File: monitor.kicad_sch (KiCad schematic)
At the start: 0 parts

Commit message: monitor changes
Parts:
- added R5: R, symbol Device:R
- added SW2: SW_Wuerth_450301014042, Button_Switch_THT:SW_Slide-03_Wuerth-WS-SLTV_10x2.5x6.4_P2.54mm, symbol Switch:SW_Wuerth_450301014042
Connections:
- net M_VIN: now also R5.1
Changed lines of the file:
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@@
 	(wire
 		(pts
-			(xy 88.9 104.14) (xy 125.73 104.14)
-		)
-		(stroke
-			(width 0)
-			(type default)
-		)
-	)
-	(wire
-		(pts
-			(xy 125.73 104.14) (xy 125.73 69.85)
+			(xy 88.9 104.14) (xy 143.51 104.14)
+		)
+		(stroke
+			(width 0)
+			(type default)
+		)
+	)
+	(wire
+		(pts
+			(xy 143.51 104.14) (xy 143.51 69.85)
 		)
 		(stroke
@@
 	(hierarchical_label "M_A1V"
 		(shape output)
-		(at 107.95 69.85 90)
+		(at 125.73 69.85 90)
 		(effects
 			(font
@@
 	(hierarchical_label "M_A2V"
 		(shape input)
-		(at 125.73 69.85 90)
+		(at 143.51 69.85 90)
 		(effects
 			(font
@@
 		)
 	)
+	(symbol
+		(lib_id "Switch:SW_Wuerth_450301014042")
+		(at 109.22 81.28 0)
+		(unit 1)
+		(exclude_from_sim no)
+		(in_bom yes)
+		(on_board yes)
+		(dnp no)
+		(fields_autoplaced yes)
+		(property "Reference" "SW2"
+			(at 109.22 72.39 0)
+			(effects
+				(font
+					(size 1.27 1.27)
+				)
+			)
+		)
+		(property "Value" "SW_Wuerth_450301014042"
+			(at 109.22 74.93 0)
+			(effects
+				(font
+					(size 1.27 1.27)
+				)
+			)
+		)
+		(property "Footprint" "Button_Switch_THT:SW_Slide-03_Wuerth-WS-SLTV_10x2.5x6.4_P2.54mm"
+			(at 109.22 91.44 0)
+			(effects
+				(font
+					(size 1.27 1.27)
+				)
+				(hide yes)
+			)
+		)
+		(property "Datasheet" "https://www.we-online.com/components/products/datasheet/450301014042.pdf"
+			(at 109.22 88.9 0)
+			(effects
+				(font
+					(size 1.27 1.27)
+				)
+				(hide yes)
+			)
+		)
+		(property "Description" "Switch slide, single pole double throw"
+			(at 109.22 81.28 0)
+			(effects
+				(font
+					(size 1.27 1.27)
+				)
+				(hide yes)
+			)
+		)
+		(pin "1"
+		)
+		(pin "2"
+		)
+		(pin "3"
+		)
+		(instances
+			(project ""
+				(path "/bdc7face-9f7c-4701-80bb-4cc144448db1/10220f6e-30e0-4da2-bc7c-0672de199a7a"
+					(reference "SW2")
+					(unit 1)
+				)
+			)
+		)
+	)
+	(symbol
+		(lib_id "Device:R")
+		(at 92.71 81.28 90)
+		(unit 1)
+		(exclude_from_sim no)
+		(in_bom yes)
+		(on_board yes)
+		(dnp no)
+		(fields_autoplaced yes)
+		(property "Reference" "R5"
+			(at 92.71 74.93 90)
+			(effects
+				(font
+					(size 1.27 1.27)
+				)
+			)
+		)
+		(property "Value" "R"
+			(at 92.71 77.47 90)
+			(effects
+				(font
+					(size 1.27 1.27)
+				)
+			)
+		)
+		(property "Footprint" ""
+			(at 92.71 83.058 90)
+			(effects
+				(font
+					(size 1.27 1.27)
+				)
+				(hide yes)
+			)
+		)
+		(property "Datasheet" "~"
+			(at 92.71 81.28 0)
+			(effects
+				(font
+					(size 1.27 1.27)
+				)
+				(hide yes)
+			)
+		)
+		(property "Description" "Resistor"
+			(at 92.71 81.28 0)
+			(effects
+				(font
+					(size 1.27 1.27)
+				)
+				(hide yes)
+			)
+		)
+		(pin "2"
+		)
+		(pin "1"
+		)
+		(instances
+			(project ""
+				(path "/bdc7face-9f7c-4701-80bb-4cc144448db1/10220f6e-30e0-4da2-bc7c-0672de199a7a"
+					(reference "R5")
+					(unit 1)
+				)
+			)
+		)
+	)

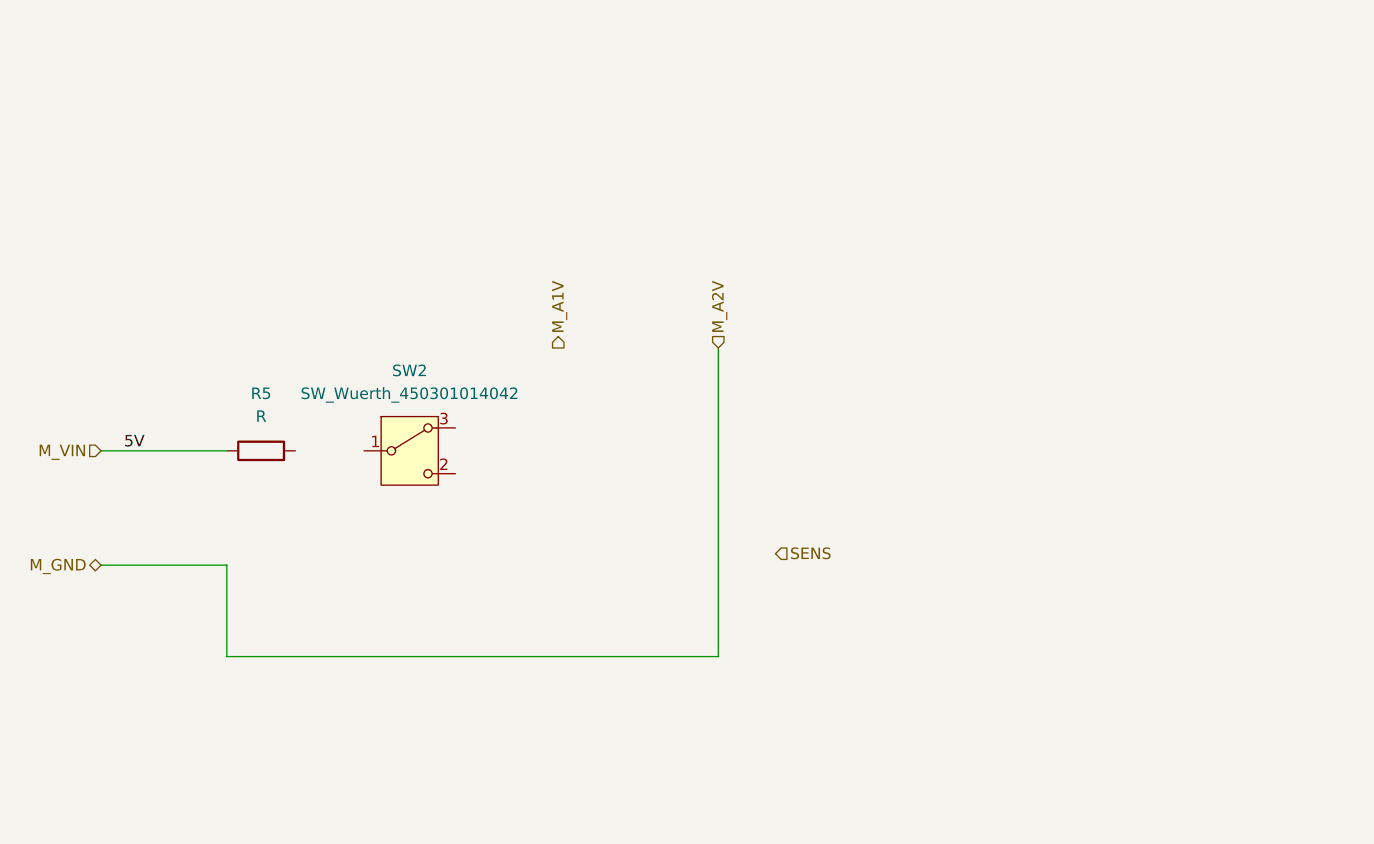
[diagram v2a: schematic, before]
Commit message: monitor internals: temporary solution
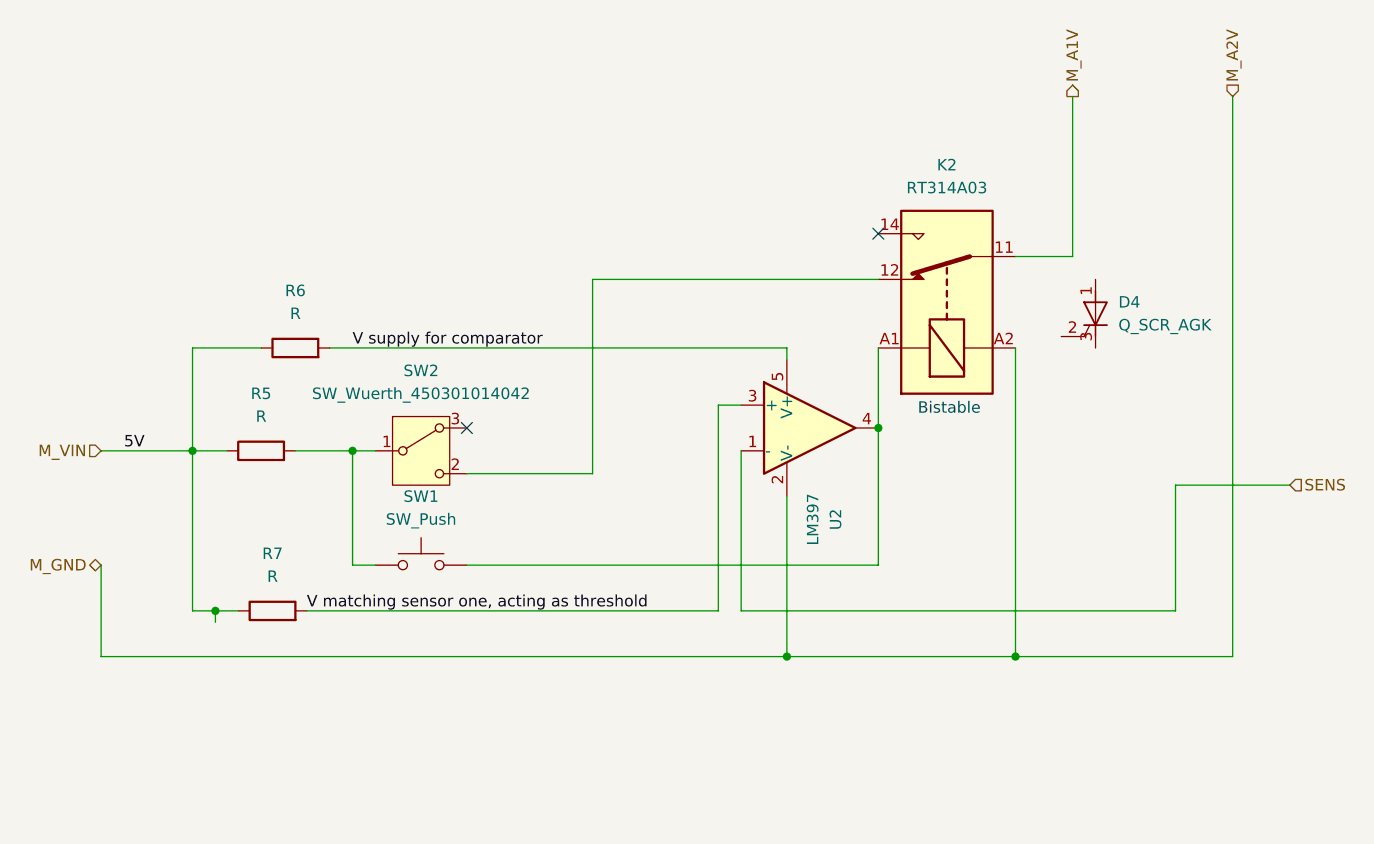
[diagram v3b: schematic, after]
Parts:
- added D4: Q_SCR_AGK, symbol Device:Q_SCR_AGK
- added K2: RT314A03, Relay_THT:Relay_SPDT_Schrack-RT1-16A-FormC_RM5mm, symbol Relay:RT314A05
- added R6, R7: R, symbol Device:R
- added SW1: SW_Push, symbol Switch:SW_Push
- added U2: LM397, Package_TO_SOT_SMD:SOT-23-5, symbol Comparator:LM397
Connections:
- net M_A1V: now also K2.11
- net M_A2V: now also K2.A2, U2.2 (V-)
- net M_VIN: now also R6.1, R7.1
- net SENS: now also U2.1 (-)
- net at SW2.1 (B): now also R5.2, SW1.1
- net at SW2.2 (C): now also K2.12
- new net: K2.A1, SW1.2, U2.4
- new net V matching sensor one, acting as threshold: R7.2, U2.3 (+)
- new net V supply for comparator: R6.2, U2.5 (V+)
- no-connect marks 0 -> 2
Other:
- note added: "Bistable"
- moved on the sheet: SW2

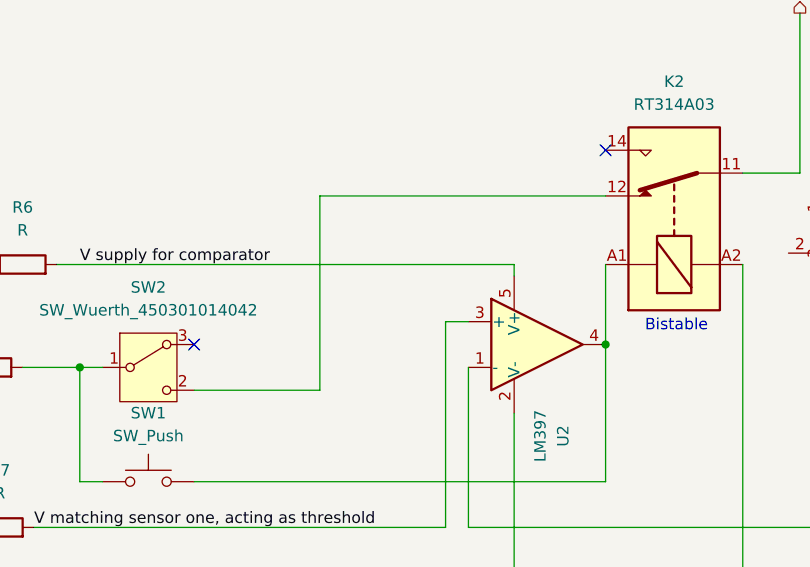
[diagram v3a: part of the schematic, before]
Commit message: corrected monitor source
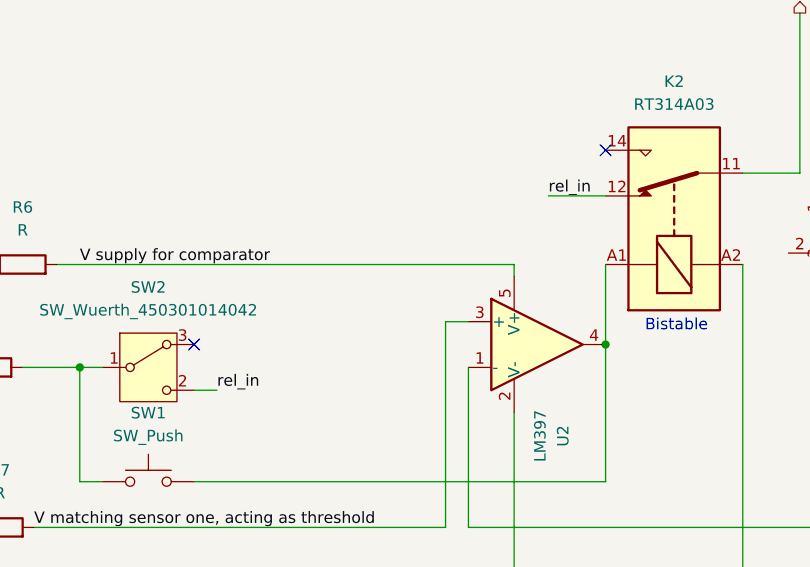
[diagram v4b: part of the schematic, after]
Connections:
- net rel_in: now reaches K2.12, SW2.2 (C)
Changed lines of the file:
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@@
 	(wire
 		(pts
-			(xy 129.54 83.82) (xy 115.57 83.82)
+			(xy 118.11 83.82) (xy 115.57 83.82)
 		)
 		(stroke
@@
 	(wire
 		(pts
-			(xy 129.54 62.23) (xy 161.29 62.23)
+			(xy 154.94 62.23) (xy 161.29 62.23)
 		)
 		(stroke
@@
 		(pts
 			(xy 87.63 100.33) (xy 87.63 99.06)
-		)
-		(stroke
-			(width 0)
-			(type default)
-		)
-	)
-	(wire
-		(pts
-			(xy 129.54 62.23) (xy 129.54 83.82)
 		)
 		(stroke
@@
 		(effects
 			(font
+				(size 1.27 1.27)
+			)
+			(justify left bottom)
+		)
+	)
+	(label "rel_in"
+		(at 118.11 83.82 0)
+		(effects
+			(font
+				(size 1.27 1.27)
+			)
+			(justify left bottom)
+		)
+	)
+	(label "rel_in"
+		(at 154.94 62.23 0)
+		(effects
+			(font

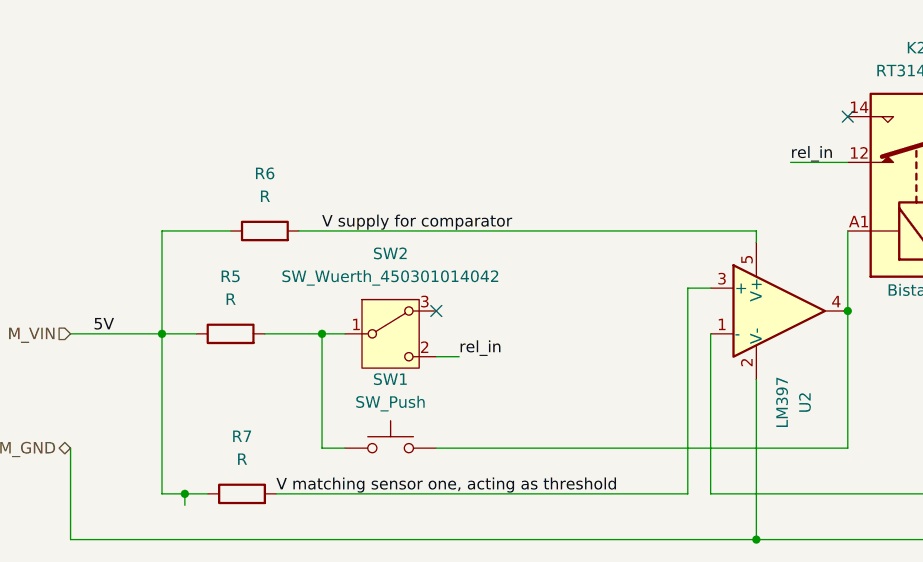
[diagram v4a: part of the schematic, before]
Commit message: added LPF and correct load LED
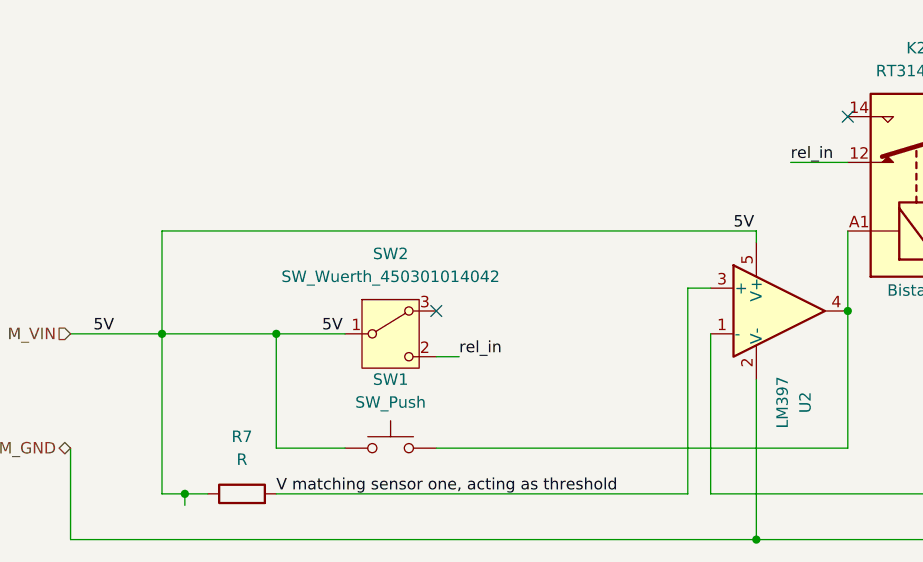
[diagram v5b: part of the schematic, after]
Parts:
- removed R5, R6: R, symbol Device:R
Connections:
- net V supply for comparator is gone; now on net M_VIN: U2.5 (V+)
- net M_VIN: now also SW1.1, SW2.1 (B)
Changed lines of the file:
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@@
-	)
-	(junction
-		(at 102.87 81.28)
-		(diameter 0)
-		(color 0 0 0 0)
 	)
 	(junction
@@
 	)
 	(junction
+		(at 97.79 81.28)
+		(diameter 0)
+		(color 0 0 0 0)
+	)
+	(junction
 		(at 151.13 104.14)
 		(diameter 0)
@@
 	(wire
 		(pts
-			(xy 85.09 69.85) (xy 92.71 69.85)
+			(xy 85.09 69.85) (xy 151.13 69.85)
 		)
 		(stroke
@@
 	(wire
 		(pts
-			(xy 102.87 93.98) (xy 105.41 93.98)
+			(xy 97.79 93.98) (xy 105.41 93.98)
 		)
 		(stroke
@@
 	(wire
 		(pts
+			(xy 97.79 81.28) (xy 105.41 81.28)
+		)
+		(stroke
+			(width 0)
+			(type default)
+		)
+	)
+	(wire
+		(pts
 			(xy 200.66 104.14) (xy 200.66 41.91)
 		)
@@
 	(wire
 		(pts
-			(xy 151.13 69.85) (xy 100.33 69.85)
-		)
-		(stroke
-			(width 0)
-			(type default)
-		)
-	)
-	(wire
-		(pts
 			(xy 207.01 85.09) (xy 194.31 85.09)
 		)
@@
 	(wire
 		(pts
-			(xy 102.87 81.28) (xy 102.87 93.98)
+			(xy 97.79 81.28) (xy 97.79 93.98)
 		)
 		(stroke
@@
 	(wire
 		(pts
-			(xy 96.52 81.28) (xy 102.87 81.28)
-		)
-		(stroke
-			(width 0)
-			(type default)
-		)
-	)
-	(wire
-		(pts
 			(xy 143.51 76.2) (xy 146.05 76.2)
 		)
@@
 	(wire
 		(pts
-			(xy 102.87 81.28) (xy 105.41 81.28)
-		)
-		(stroke
-			(width 0)
-			(type default)
-		)
-	)
-	(wire
-		(pts
 			(xy 161.29 78.74) (xy 161.29 69.85)
 		)
@@
 	(wire
 		(pts
-			(xy 85.09 81.28) (xy 88.9 81.28)
-		)
-		(stroke
-			(width 0)
-			(type default)
-		)
-	)
-	(label "V supply for comparator"
-		(at 102.87 69.85 0)
+			(xy 85.09 81.28) (xy 97.79 81.28)
+		)
+		(stroke
+			(width 0)
+			(type default)
+		)
+	)
+	(label "5V"
+		(at 148.59 69.85 0)
 		(effects
 			(font
@@
 	(label "V matching sensor one, acting as threshold"
 		(at 97.79 99.06 0)
+		(effects
+			(font
+				(size 1.27 1.27)
+			)
+			(justify left bottom)
+		)
+	)
+	(label "5V"
+		(at 102.87 81.28 0)
 		(effects
 			(font
@@
 			)
 			(justify left)
-		)
-	)
-	(symbol
-		(lib_id "Device:R")
-		(at 96.52 69.85 90)
-		(unit 1)
-		(exclude_from_sim no)
-		(in_bom yes)
-		(on_board yes)
-		(dnp no)
-		(fields_autoplaced yes)
-		(property "Reference" "R6"
-			(at 96.52 63.5 90)
-			(effects
-				(font
-					(size 1.27 1.27)
-				)
-			)
-		)
-		(property "Value" "R"
-			(at 96.52 66.04 90)
-			(effects
-				(font
-					(size 1.27 1.27)
-				)
-			)
-		)
-		(property "Footprint" ""
-			(at 96.52 71.628 90)
-			(effects
-				(font
-					(size 1.27 1.27)
-				)
-				(hide yes)
-			)
-		)
-		(property "Datasheet" "~"
-			(at 96.52 69.85 0)
-			(effects
-				(font
-					(size 1.27 1.27)
-				)
-				(hide yes)
-			)
-		)
-		(property "Description" "Resistor"
-			(at 96.52 69.85 0)
-			(effects
-				(font
-					(size 1.27 1.27)
-				)
-				(hide yes)
-			)
-		)
-		(pin "2"
-		)
-		(pin "1"
-		)
-		(instances
-			(project "recruitment"
-				(path "/bdc7face-9f7c-4701-80bb-4cc144448db1/10220f6e-30e0-4da2-bc7c-0672de199a7a"
-					(reference "R6")
-					(unit 1)
-				)
-			)
 		)
 	)
@@
 					(unit 1)
 				)
-			)
-		)
-	)
-	(symbol
-		(lib_id "Device:R")
-		(at 92.71 81.28 90)
-		(unit 1)
-		(exclude_from_sim no)
-		(in_bom yes)
-		(on_board yes)
-		(dnp no)
-		(fields_autoplaced yes)
-		(property "Reference" "R5"
-			(at 92.71 74.93 90)
-			(effects
-				(font
-					(size 1.27 1.27)
-				)
-			)
-		)
-		(property "Value" "R"
-			(at 92.71 77.47 90)
-			(effects
-				(font
-					(size 1.27 1.27)
-				)
-			)
-		)
-		(property "Footprint" ""
-			(at 92.71 83.058 90)
-			(effects
-				(font
-					(size 1.27 1.27)
-				)
-				(hide yes)
-			)
-		)
-		(property "Datasheet" "~"
-			(at 92.71 81.28 0)
-			(effects
-				(font
-					(size 1.27 1.27)
-				)
-				(hide yes)
-			)
-		)
-		(property "Description" "Resistor"
-			(at 92.71 81.28 0)
-			(effects
-				(font
-					(size 1.27 1.27)
-				)
-				(hide yes)
-			)
-		)
-		(pin "2"
-		)
-		(pin "1"
-		)
-		(instances
-			(project ""
-				(path "/bdc7face-9f7c-4701-80bb-4cc144448db1/10220f6e-30e0-4da2-bc7c-0672de199a7a"
-					(reference "R5")
-					(unit 1)
-				)
